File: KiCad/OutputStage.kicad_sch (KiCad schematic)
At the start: 18 parts, among them J2 Conn_Coaxial, Q1 BC547, Q2 BC557, U3 NE5532

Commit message: Added elements values
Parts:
- C10: value C -> 3,3p
- C8, C9: value C -> 100n
- R10, R8: value R -> 1k
- R11, R12: value R -> 3,3
- R4: value R -> 20k
- R5, R6: value R -> 680
- R7: value R -> 27
- R9: value R_Variable -> 100
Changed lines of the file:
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@@
 			)
 		)
-		(property "Value" "R"
+		(property "Value" "20k"
 			(at 115.57 105.4099 0)
 			(effects
@@
 			)
 		)
-		(property "Value" "C"
+		(property "Value" "100n"
 			(at 54.61 71.1199 0)
 			(effects
@@
 			)
 		)
-		(property "Value" "C"
+		(property "Value" "100n"
 			(at 54.61 60.9599 0)
 			(effects
@@
 			)
 		)
-		(property "Value" "R"
+		(property "Value" "27"
 			(at 147.32 93.98 90)
 			(effects
@@
 			)
 		)
-		(property "Value" "R"
+		(property "Value" "3,3"
 			(at 180.34 91.4399 0)
 			(effects
@@
 			)
 		)
-		(property "Value" "R"
+		(property "Value" "680"
 			(at 132.08 107.95 90)
 			(effects
@@
 			)
 		)
-		(property "Value" "R"
+		(property "Value" "1k"
 			(at 157.48 73.6599 0)
 			(effects
@@
 			)
 		)
-		(property "Value" "C"
+		(property "Value" "3,3p"
 			(at 106.68 105.4099 0)
 			(effects
@@
 			)
 		)
-		(property "Value" "R"
+		(property "Value" "680"
 			(at 124.46 121.9199 0)
 			(effects
@@
 			)
 		)
-		(property "Value" "R"
+		(property "Value" "3,3"
 			(at 180.34 106.6799 0)
 			(effects
@@
 			)
 		)
-		(property "Value" "R"
+		(property "Value" "1k"
 			(at 157.48 125.7299 0)
 			(effects
@@
 			)
 		)
-		(property "Value" "R_Variable"
+		(property "Value" "100"
 			(at 158.75 104.1399 0)
 			(effects

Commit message: Filled in schematic
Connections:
- net DAC_OUT renamed DAC_IN
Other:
- note added: "OpAmp Power"
- note added: "Output Amplifier"
- moved on the sheet: C8, C9, U3C

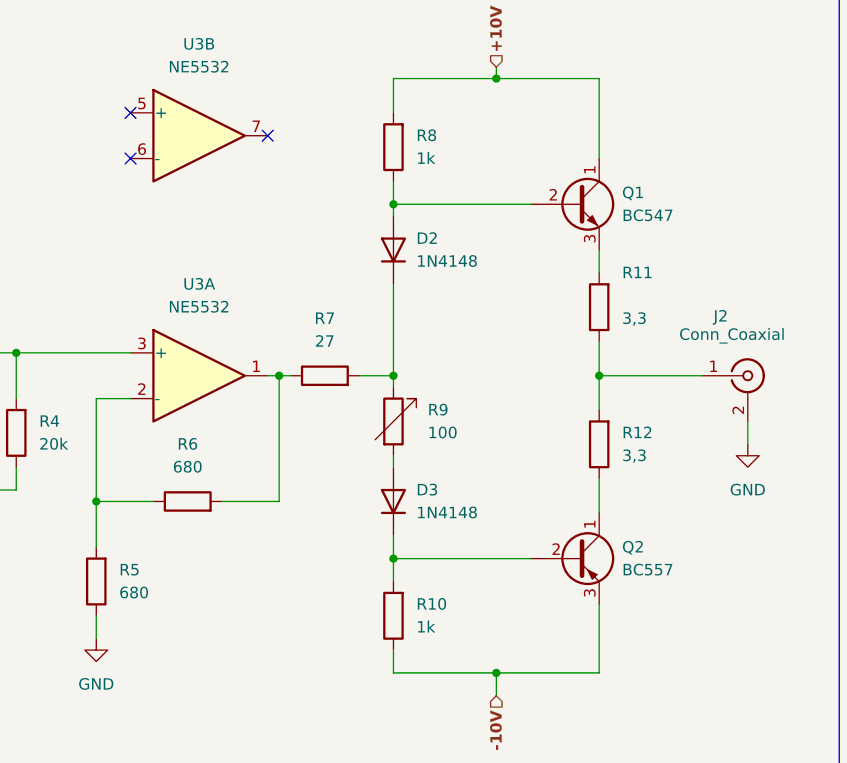
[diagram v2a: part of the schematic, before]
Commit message: Added footprints
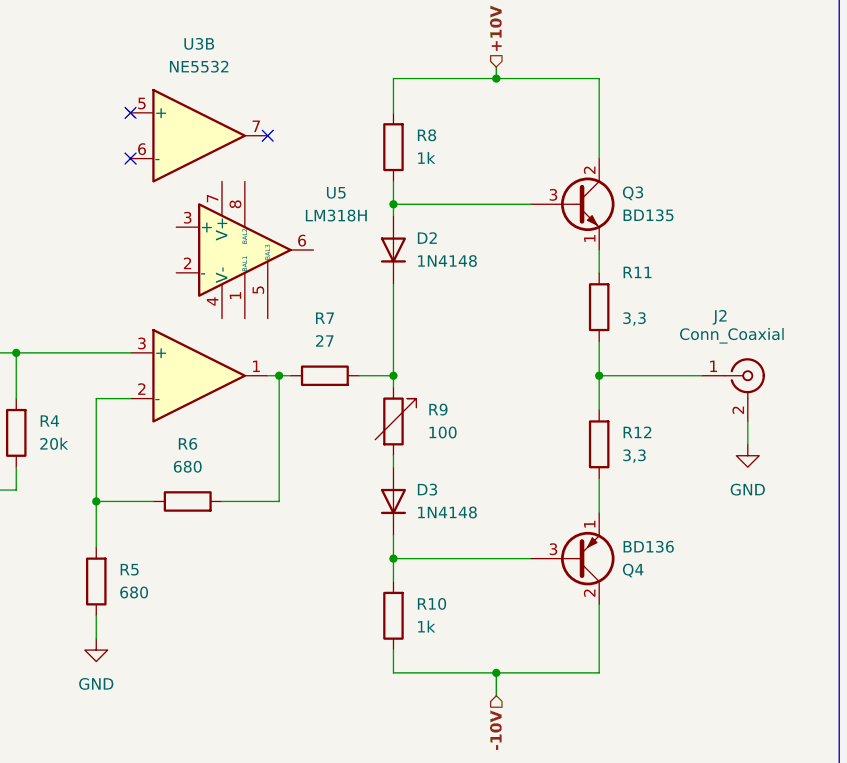
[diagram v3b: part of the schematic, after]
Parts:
- removed Q1: BC547, Package_TO_SOT_THT:TO-92_HandSolder, symbol Transistor_BJT:BC547
- removed Q2: BC557, Package_TO_SOT_THT:TO-92_HandSolder, symbol Transistor_BJT:BC557
- added Q3: BD135, Package_TO_SOT_THT:TO-126-3_Vertical, symbol Transistor_BJT:BD135
- added Q4: BD136, Package_TO_SOT_THT:TO-126-3_Vertical, symbol Transistor_BJT:BD136
- added U5: LM318H, Package_DIP:DIP-8_W7.62mm, symbol Amplifier_Operational:LM318H
- C10, C8, C9: footprint (none) -> Capacitor_SMD:C_0805_2012Metric_Pad1.18x1.45mm_HandSolder
- R10, R11, R12, R4, R5, R6, R7, R8: footprint (none) -> Resistor_SMD:R_0805_2012Metric_Pad1.20x1.40mm_HandSolder
- R9: footprint (none) -> Potentiometer_THT:Potentiometer_ACP_CA9-V10_Vertical
- U3: footprint Package_DIP:DIP-8_W7.62mm_Socket_LongPads -> (none)
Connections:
- net +10V: now also Q3.2 (C)
- net -10V: now also Q4.2 (C)
- net at R11.2: now also Q3.1 (E)
- net at R12.1: now also Q4.1 (E)
- net at D3.1 (K), R10.2: now also Q4.3 (B)
- net at D2.2 (A), R8.1: now also Q3.3 (B)

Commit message: minor changes
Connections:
- no-connect marks 3 -> 6
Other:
- moved on the sheet: U3B, U5
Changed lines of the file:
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@@
 	)
 	(no_connect
-		(at 140.97 71.12)
+		(at 138.43 76.2)
 	)
 	(no_connect
-		(at 125.73 73.66)
+		(at 123.19 78.74)
 	)
 	(no_connect
-		(at 125.73 68.58)
+		(at 106.68 67.31)
+	)
+	(no_connect
+		(at 123.19 73.66)
+	)
+	(no_connect
+		(at 106.68 82.55)
+	)
+	(no_connect
+		(at 109.22 82.55)
 	)
 	(wire
@@
 	(symbol
 		(lib_id "Amplifier_Operational:NE5532")
-		(at 133.35 71.12 0)
+		(at 130.81 76.2 0)
 		(unit 2)
 		(exclude_from_sim no)
@@
 		(fields_autoplaced yes)
 		(property "Reference" "U3"
-			(at 133.35 60.96 0)
+			(at 130.81 66.04 0)
 			(effects
 				(font
@@
 		)
 		(property "Value" "NE5532"
-			(at 133.35 63.5 0)
+			(at 130.81 68.58 0)
 			(effects
 				(font
@@
 		)
 		(property "Footprint" ""
-			(at 133.35 71.12 0)
+			(at 130.81 76.2 0)
 			(effects
 				(font
@@
 		)
 		(property "Datasheet" "http://www.ti.com/lit/ds/symlink/ne5532.pdf"
-			(at 133.35 71.12 0)
+			(at 130.81 76.2 0)
 			(effects
 				(font
@@
 		)
 		(property "Description" "Dual Low-Noise Operational Amplifiers, DIP-8/SOIC-8"
-			(at 133.35 71.12 0)
+			(at 130.81 76.2 0)
 			(effects
 				(font
@@
 	(symbol
 		(lib_id "Amplifier_Operational:LM318H")
-		(at 138.43 83.82 0)
+		(at 106.68 74.93 0)
 		(unit 1)
 		(exclude_from_sim no)
@@
 		(fields_autoplaced yes)
 		(property "Reference" "U5"
-			(at 148.59 77.5014 0)
+			(at 116.84 68.6114 0)
 			(effects
 				(font
@@
 		)
 		(property "Value" "LM318H"
-			(at 148.59 80.0414 0)
+			(at 116.84 71.1514 0)
 			(effects
 				(font
@@
 		)
 		(property "Footprint" "Package_DIP:DIP-8_W7.62mm"
-			(at 138.43 83.82 0)
+			(at 106.68 74.93 0)
 			(effects
 				(font
@@
 		)
 		(property "Datasheet" "http://www.ti.com/lit/ds/symlink/lm318-n.pdf"
-			(at 138.43 83.82 0)
+			(at 106.68 74.93 0)
 			(effects
 				(font
@@
 		)
 		(property "Description" "Operational Amplifier, TO-99-8"
-			(at 138.43 83.82 0)
-			(effects
-				(font
+			(at 106.68 74.93 0)
+			(effects
+				(font

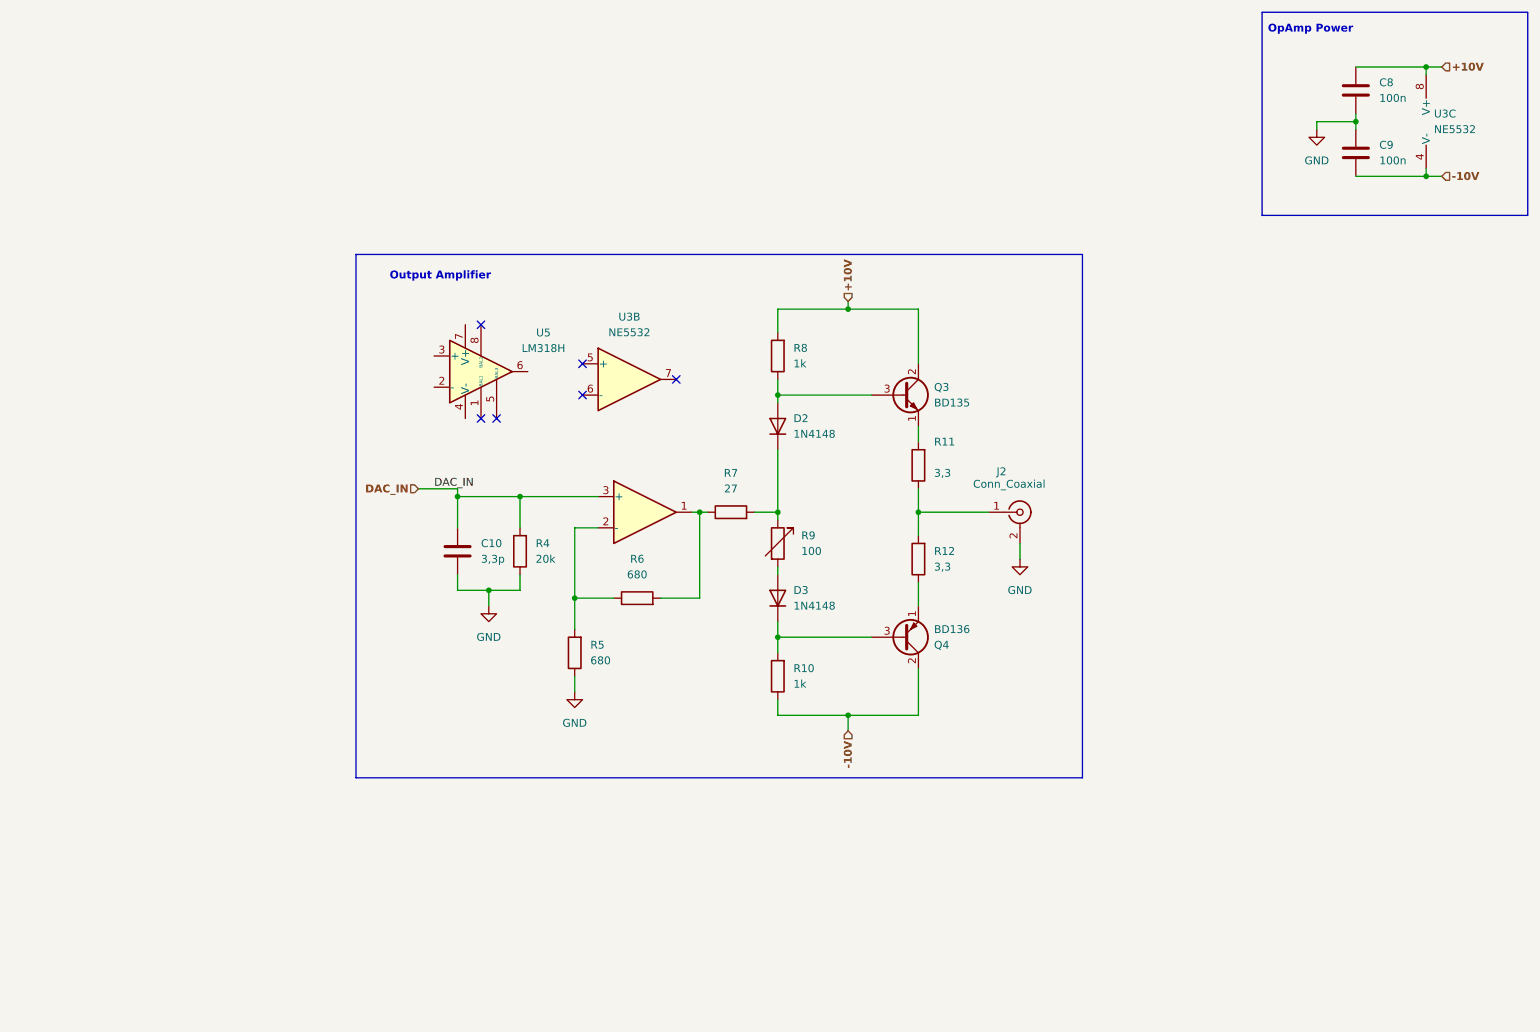
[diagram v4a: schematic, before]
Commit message: UI connections to uC
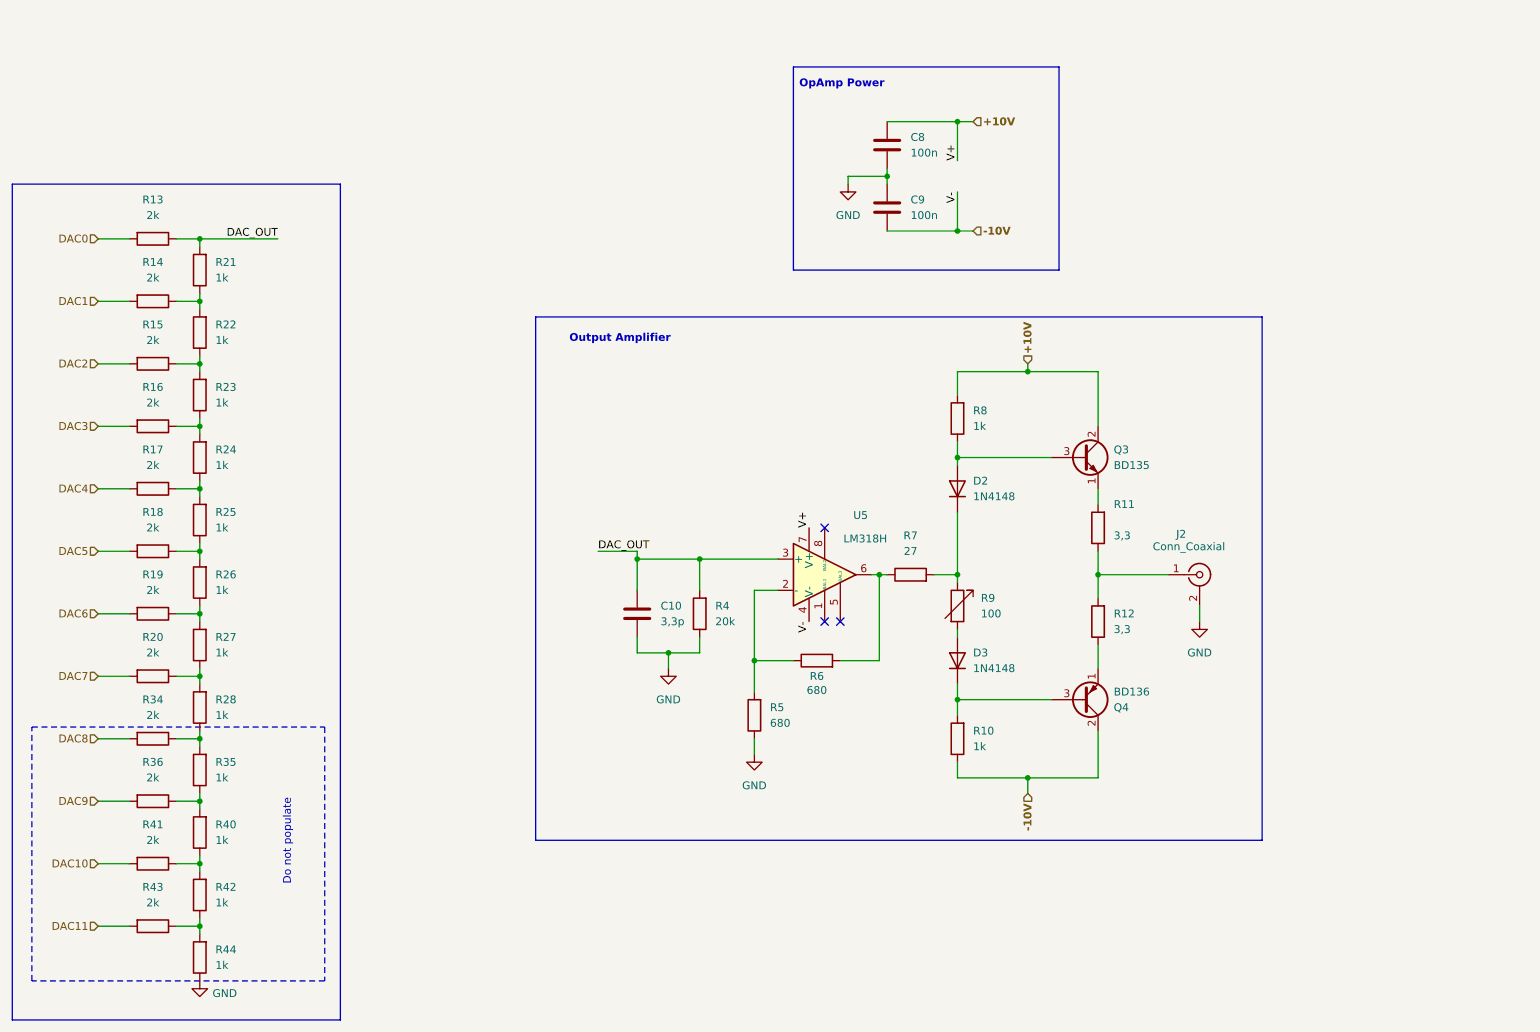
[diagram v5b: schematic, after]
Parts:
- removed U3: NE5532, symbol Amplifier_Operational:NE5532
- added R13, R14, R15, R16, R17, R18, R19, R20, R34, R36, R41, R43: 2k, Resistor_SMD:R_0805_2012Metric_Pad1.20x1.40mm_HandSolder, symbol Device:R
- added R21, R22, R23, R24, R25, R26, R27, R28, R35, R40, R42, R44: 1k, Resistor_SMD:R_0805_2012Metric_Pad1.20x1.40mm_HandSolder, symbol Device:R
- J2: footprint (none) -> Connector_Coaxial:BNC_Amphenol_B6252HB-NPP3G-50_Horizontal
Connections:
- net DAC_IN is gone; now on net DAC_OUT: C10.1, R4.2
- net +10V: now also U5.7 (V+)
- net -10V: now also U5.4 (V-)
- net GND: now also R44.1
- net at R6.2, R7.1: now also U5.6
- net at U5.2 (-): now also R5.2, R6.1
- net DAC_OUT: now reaches U5.3 (+)
- net DAC_OUT: now also R13.1, R21.2
- new net: R14.1, R21.1, R22.2
- new net: R15.1, R22.1, R23.2
- new net: R16.1, R23.1, R24.2
- new net: R42.1, R43.1, R44.2
- new net: R40.1, R41.1, R42.2
- new net: R35.1, R36.1, R40.2
- new net: R19.1, R26.1, R27.2
- new net: R18.1, R25.1, R26.2
- new net: R17.1, R24.1, R25.2
- new net: R28.1, R34.1, R35.2
- new net: R20.1, R27.1, R28.2
- new net DAC0: R13.2
- new net DAC1: R14.2
- new net DAC10: R41.2
- new net DAC11: R43.2
- new net DAC2: R15.2
- new net DAC3: R16.2
- new net DAC4: R17.2
- new net DAC5: R18.2
- new net DAC6: R19.2
- new net DAC7: R20.2
- new net DAC8: R34.2
- new net DAC9: R36.2
- no-connect marks 6 -> 3
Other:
- note added: "Do not populate"
- moved on the sheet: C10, C8, C9, D2, D3, J2, Q3, Q4, R10, R11, R12, R4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

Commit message: First DAC layout, rough board layout
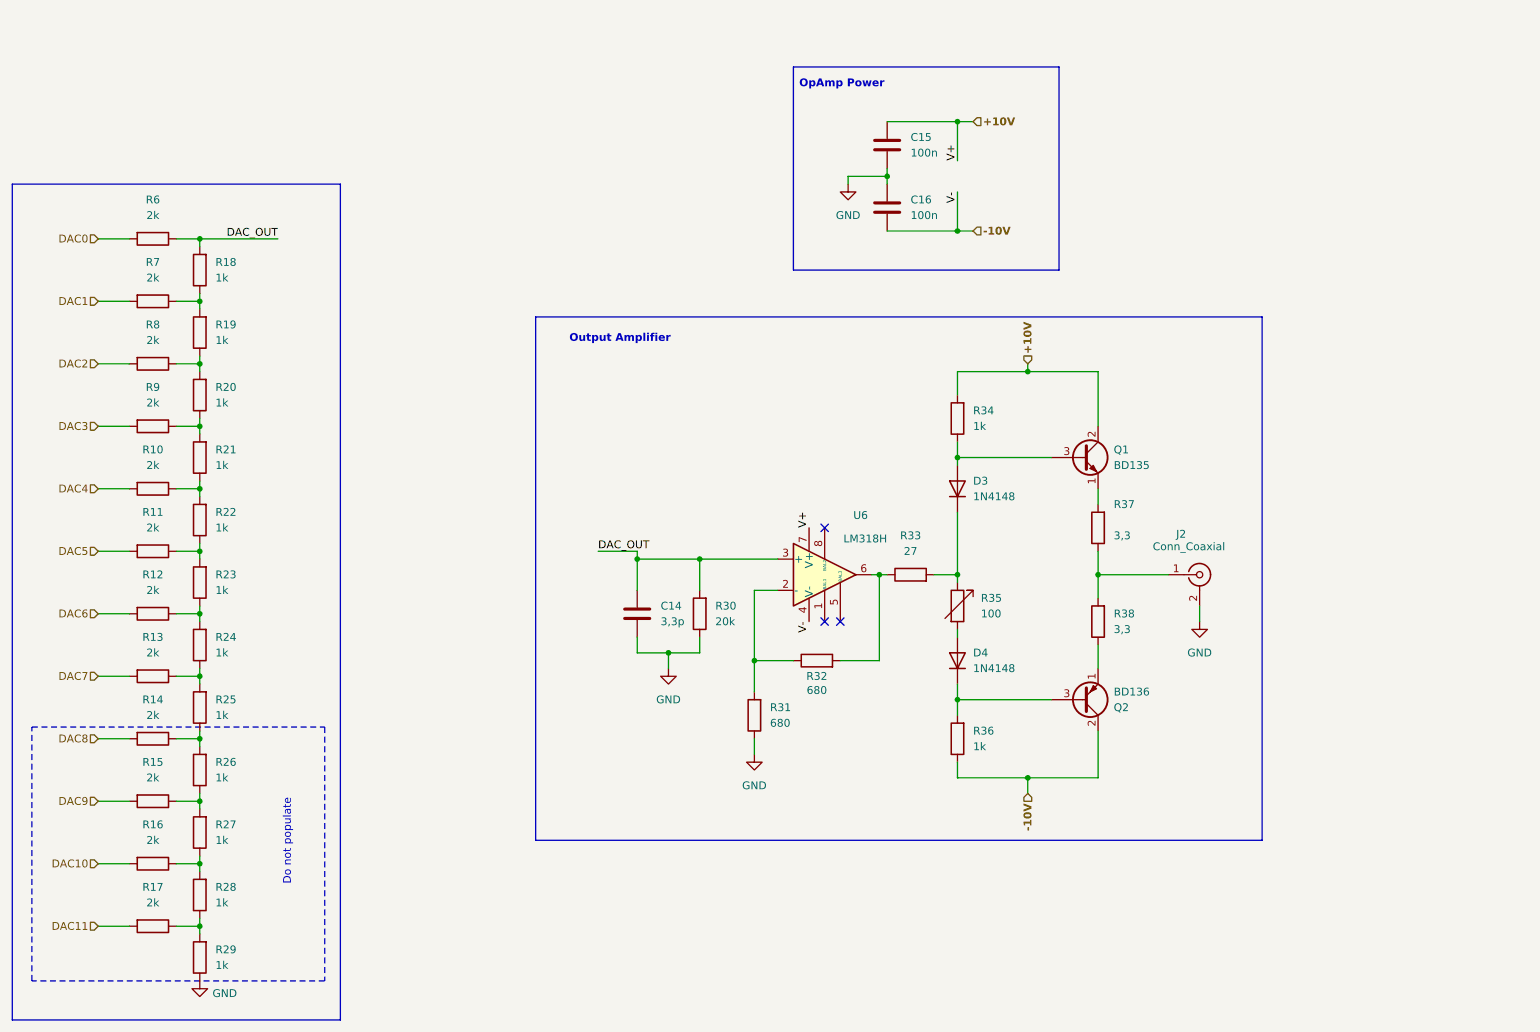
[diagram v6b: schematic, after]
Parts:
- renumbered C10 to C14, C8 to C15, C9 to C16, D2 to D3, D3 to D4, Q3 to Q1, Q4 to Q2, R17 to R10, R18 to R11, R19 to R12, R20 to R13, R34 to R14, R36 to R15, R41 to R16, R43 to R17, R21 to R18, R22 to R19, R23 to R20, R24 to R21, R25 to R22, R26 to R23, R27 to R24, R28 to R25, R35 to R26, R40 to R27, R42 to R28, R44 to R29, R4 to R30, R5 to R31, R6 to R32, R7 to R33, R8 to R34, R9 to R35, R10 to R36, R11 to R37, R12 to R38, R13 to R6, R14 to R7, R15 to R8, R16 to R9, U5 to U6

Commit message: minor changes, testing
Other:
- moved on the sheet: C14, C15, C16, D3, D4, J2, Q1, Q2, R30, R31, R32, R33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

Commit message: Changed footprints, arrangement of elements on pcb
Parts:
- D3, D4: footprint Diode_THT:D_DO-35_SOD27_P7.62mm_Horizontal -> Diode_SMD:Nexperia_CFP3_SOD-123W
- R37, R38: footprint Resistor_SMD:R_0805_2012Metric_Pad1.20x1.40mm_HandSolder -> Resistor_SMD:R_2512_6332Metric_Pad1.40x3.35mm_HandSolder
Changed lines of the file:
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@@
 			)
 		)
-		(property "Footprint" "Resistor_SMD:R_0805_2012Metric_Pad1.20x1.40mm_HandSolder"
+		(property "Footprint" "Resistor_SMD:R_2512_6332Metric_Pad1.40x3.35mm_HandSolder"
 			(at 187.198 100.33 90)
 			(effects
@@
 			)
 		)
-		(property "Footprint" "Diode_THT:D_DO-35_SOD27_P7.62mm_Horizontal"
+		(property "Footprint" "Diode_SMD:Nexperia_CFP3_SOD-123W"
 			(at 162.56 121.92 0)
 			(effects
@@
 			)
 		)
-		(property "Footprint" "Diode_THT:D_DO-35_SOD27_P7.62mm_Horizontal"
+		(property "Footprint" "Diode_SMD:Nexperia_CFP3_SOD-123W"
 			(at 162.56 93.98 0)
 			(effects
@@
 			)
 		)
-		(property "Footprint" "Resistor_SMD:R_0805_2012Metric_Pad1.20x1.40mm_HandSolder"
+		(property "Footprint" "Resistor_SMD:R_2512_6332Metric_Pad1.40x3.35mm_HandSolder"
 			(at 187.198 115.57 90)
 			(effects
